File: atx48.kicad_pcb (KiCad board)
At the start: 2 copper layers, 148.9 x 85.2 mm, 87 parts, among them J1 XT60, J2 ATX-24, J3 Conn_02x02_Top_Bottom, J4 Conn_02x02_Top_Bottom, Q2 KIA3510AD, Q5 2N7002, Q6 2N7002, U1 Brick-DCDC, U10 ZXDN10, U2 LM5067, U3 EL3H7(B)(TA)-G, U4 EL3H7(B)(TA)-G, U5 AV10-48S05, U6 EL3H7(B)(TA)-G, U7 TPS3510, U8 ZXDN10, U9 ZXDN10

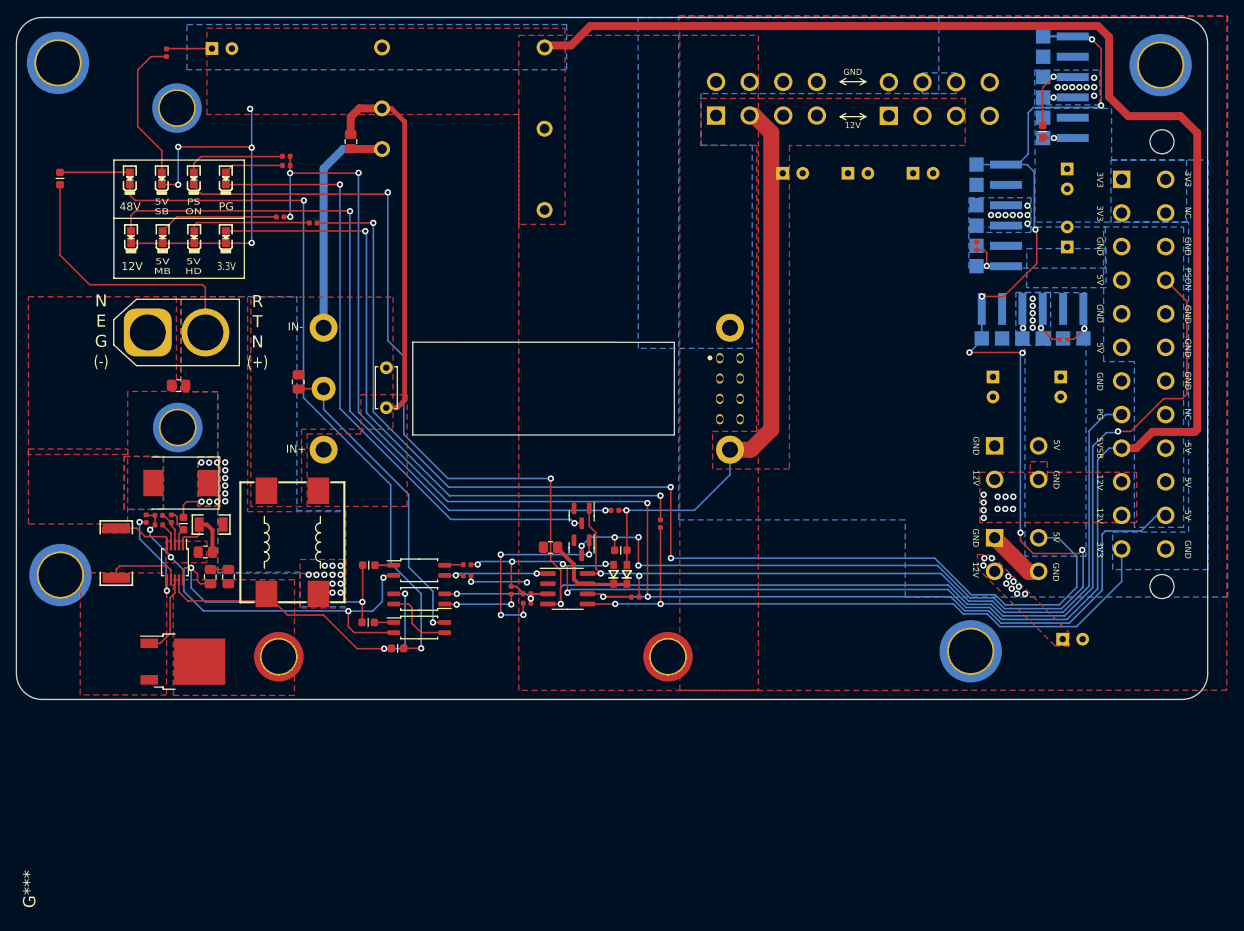
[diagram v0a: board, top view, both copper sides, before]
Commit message: Add filter capacitors; add Y cap
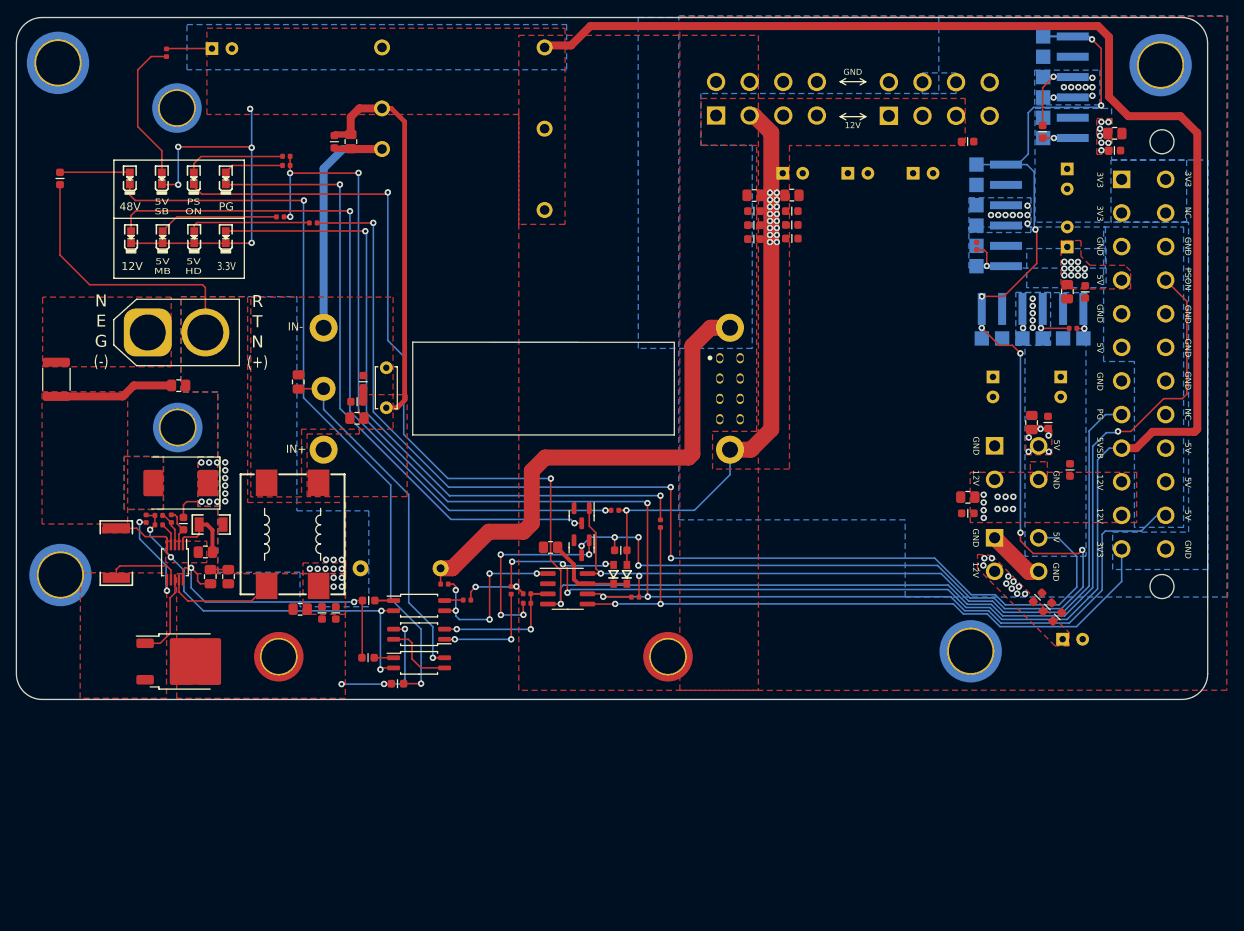
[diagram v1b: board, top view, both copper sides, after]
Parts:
- removed G*** (x2): LOGO, LOGO
- added C18: 10nF/100V, lc:0603_C, F.Cu at (128.7, 98.5)
- added C19: 10nF/100V, lc:0603_C, F.Cu at (126.0, 124.9)
- added C20: 100nF/100V, lc:0805_C, F.Cu at (121.6, 124.4)
- added C21: 10nF/100V, lc:0603_C, F.Cu at (124.3, 124.9)
- added C22: 10nF/100V, lc:0603_C, F.Cu at (125.8, 66.0)
- added C23: 10nF, lc:0603_C, F.Cu at (205.0, 112.5)
- added C24: 10nF, lc:0603_C, F.Cu at (178.3, 74.7)
- added C25: 100nF, lc:0805_C, F.Cu at (205.0, 110.5)
- added C26: 100nF, lc:0805_C, F.Cu at (178.3, 72.7)
- added C27: 100nF/100V, lc:0805_C, F.Cu at (128.7, 100.6)
- added C28: 10nF/100V, lc:0603_C, F.Cu at (129.4, 96.0)
- added C29: 10nF, lc:0603_C, F.Cu at (215.1, 101.1)
- added C30: 100nF, lc:0805_C, F.Cu at (213.0, 101.1)
- added C31: 10nF, lc:0603_C, F.Cu at (219.7, 84.8)
- added C32: 100nF, lc:0805_C, F.Cu at (217.4, 84.8)
- added C33: 10nF, lc:0603_C, F.Cu at (223.3, 67.1)
- added C34: 100nF, lc:0805_C, F.Cu at (223.4, 65.0)
- added C35: 10nF, lc:0603_C, F.Cu at (205.0, 66.0)
- added C36: 10nF, lc:0603_C, F.Cu at (217.8, 107.1)
- added C37: 10nF, lc:0603_C, F.Cu at (213.8, 123.0)
- added C38: 10nF, lc:0603_C, F.Cu at (178.3, 78.2)
- added C39: 10nF, lc:0603_C, F.Cu at (178.3, 76.5)
- added C40: 10nF, lc:0603_C, F.Cu at (215.0, 124.2)
- added C41: 10nF, lc:0603_C, F.Cu at (216.2, 125.4)
- added C42: 1nF Y1, Capacitor_THT:C_Disc_D8.0mm_W5.0mm_P10.00mm, B.Cu at (129.1, 119.3)
- added C43: 10nF, lc:0603_C, F.Cu at (183.0, 74.7)
- added C44: 10nF, lc:0603_C, F.Cu at (183.0, 76.4)
- added C45: 100nF, lc:0805_C, F.Cu at (183.0, 72.7)
- added C46: 10nF, lc:0603_C, F.Cu at (183.0, 78.1)
- added F1: T10A, Fuse:Fuse_1812_4532Metric, F.Cu at (91.1, 95.7)
- FL1: value ACM1513F-551T100 -> ACM1513F-301T130
- moved R16 4.42 mm to (130.1, 130.5)
- moved R17 4.42 mm to (130.1, 123.4)
- moved U4 4.42 mm to (136.4, 127.6)
- moved U6 4.42 mm to (136.4, 124.0)
- moved R21 4.42 mm to (142.4, 123.3)
- moved R9 4.42 mm to (133.7, 133.8)
- moved U3 4.42 mm to (136.4, 131.2)
- moved R19 3.04 mm to (139.6, 121.3), turned to 180 degrees
- moved R27 1.79 mm to (218.2, 89.3)
- moved FL1 1.00 mm to (120.6, 115.1)
- moved Q2 0.32 mm to (107.2, 131.0)
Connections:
- J1 pad 1: VEE -> Net-(J1-Pin_1)
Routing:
- net GND2: track 72.6 -> 127.8 mm, vias 32 -> 29
- net VEE: track 60.7 -> 73.4 mm
- net GND1: track 42.3 -> 30.5 mm, vias 2 -> 3
- net Net-(U7-PGI): track 13.9 -> 23.6 mm, vias 2 -> 5
- net Net-(D4-K): track 87.6 -> 92.0 mm
- net /GATE: track 39.5 -> 43.9 mm
- net Net-(R20-Pad2): track 9.68 -> 14.0 mm
- net /RTN_FIL: track 47.6 -> 51.4 mm
- net /FPO: track 14.4 -> 17.4 mm
- net /NEG_FIL: track 32.2 -> 34.2 mm
- net /DCDC_EN: track 188.4 -> 186.7 mm
- net Net-(U10-ADJ): track 6.34 -> 4.65 mm
- net /+5VSB: track 261.7 -> 263.4 mm, vias 5 -> 6
- net +5VD: vias 3 -> 8
- net +5VA: vias 6 -> 17
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- added copper zone on F.Cu, net +3.3V
- added copper zone on F.Cu, net +5VA
- added copper zone on F.Cu, net +5VD
- added copper zone on F.Cu, net Net-(J1-Pin_1)
